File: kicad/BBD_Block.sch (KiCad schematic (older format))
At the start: 70 parts, among them U301 MN3102, U302 MN3102, U303 MN3205, U304 MN3205, U305 ADG619BRMZ, U306 MN3102, U307 MN3102, U308 MN3205, U309 MN3205, U310 ADG619BRMZ

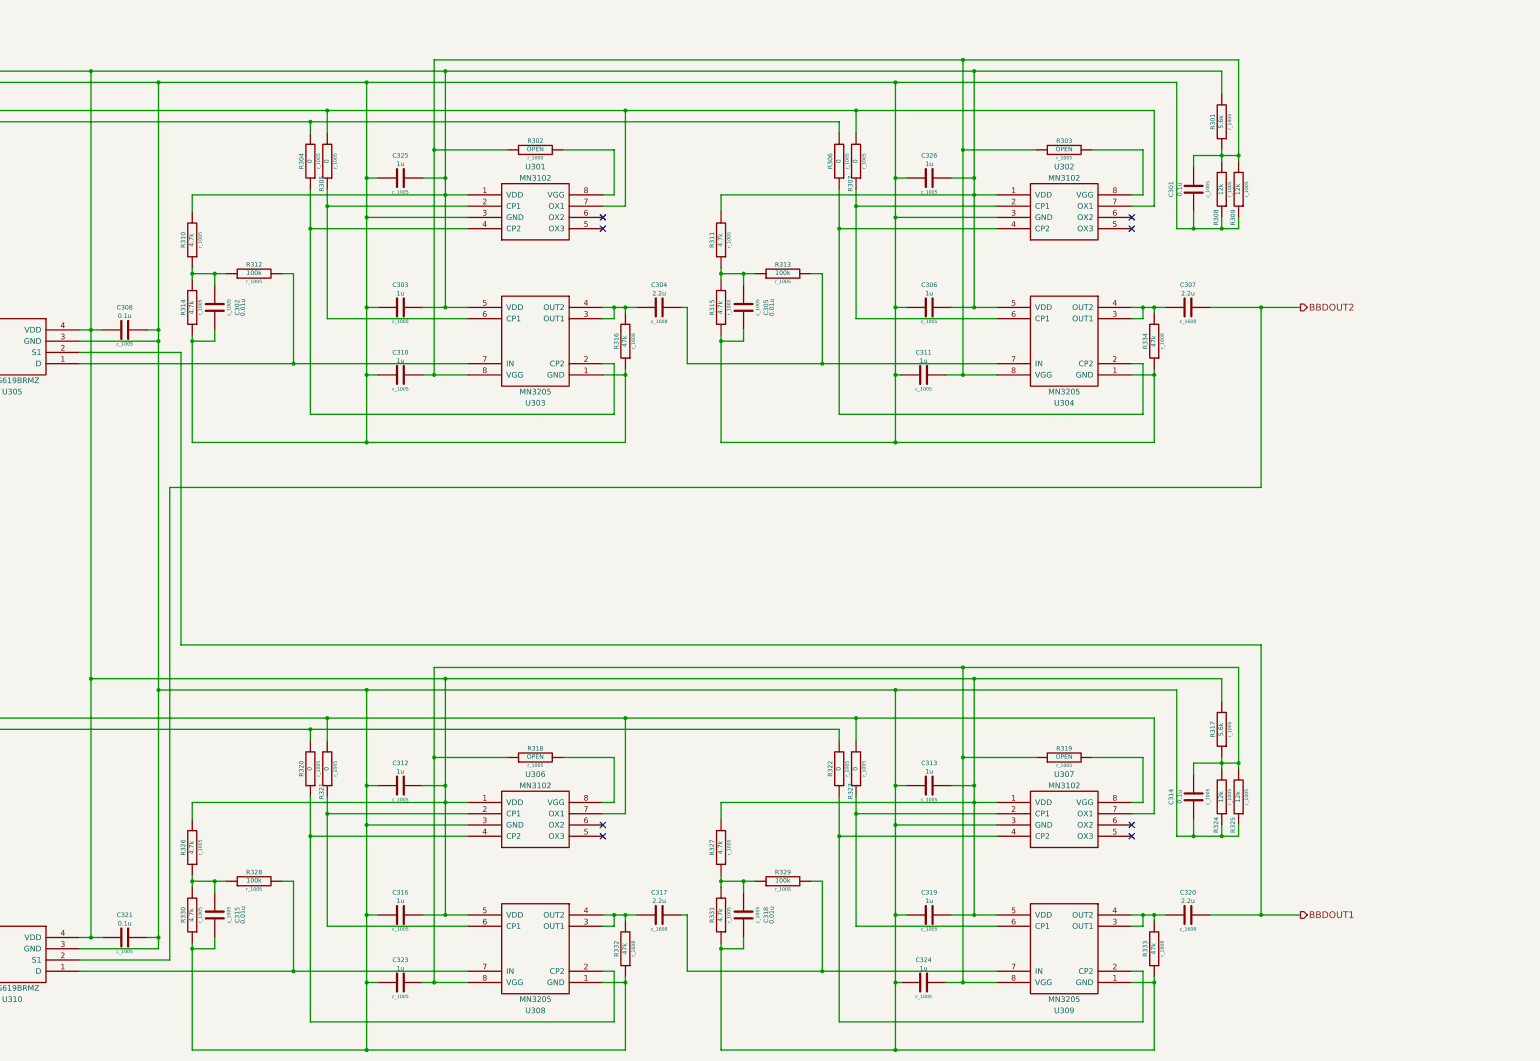
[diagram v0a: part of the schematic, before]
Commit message: Add: compander sch&pcb mod: constants
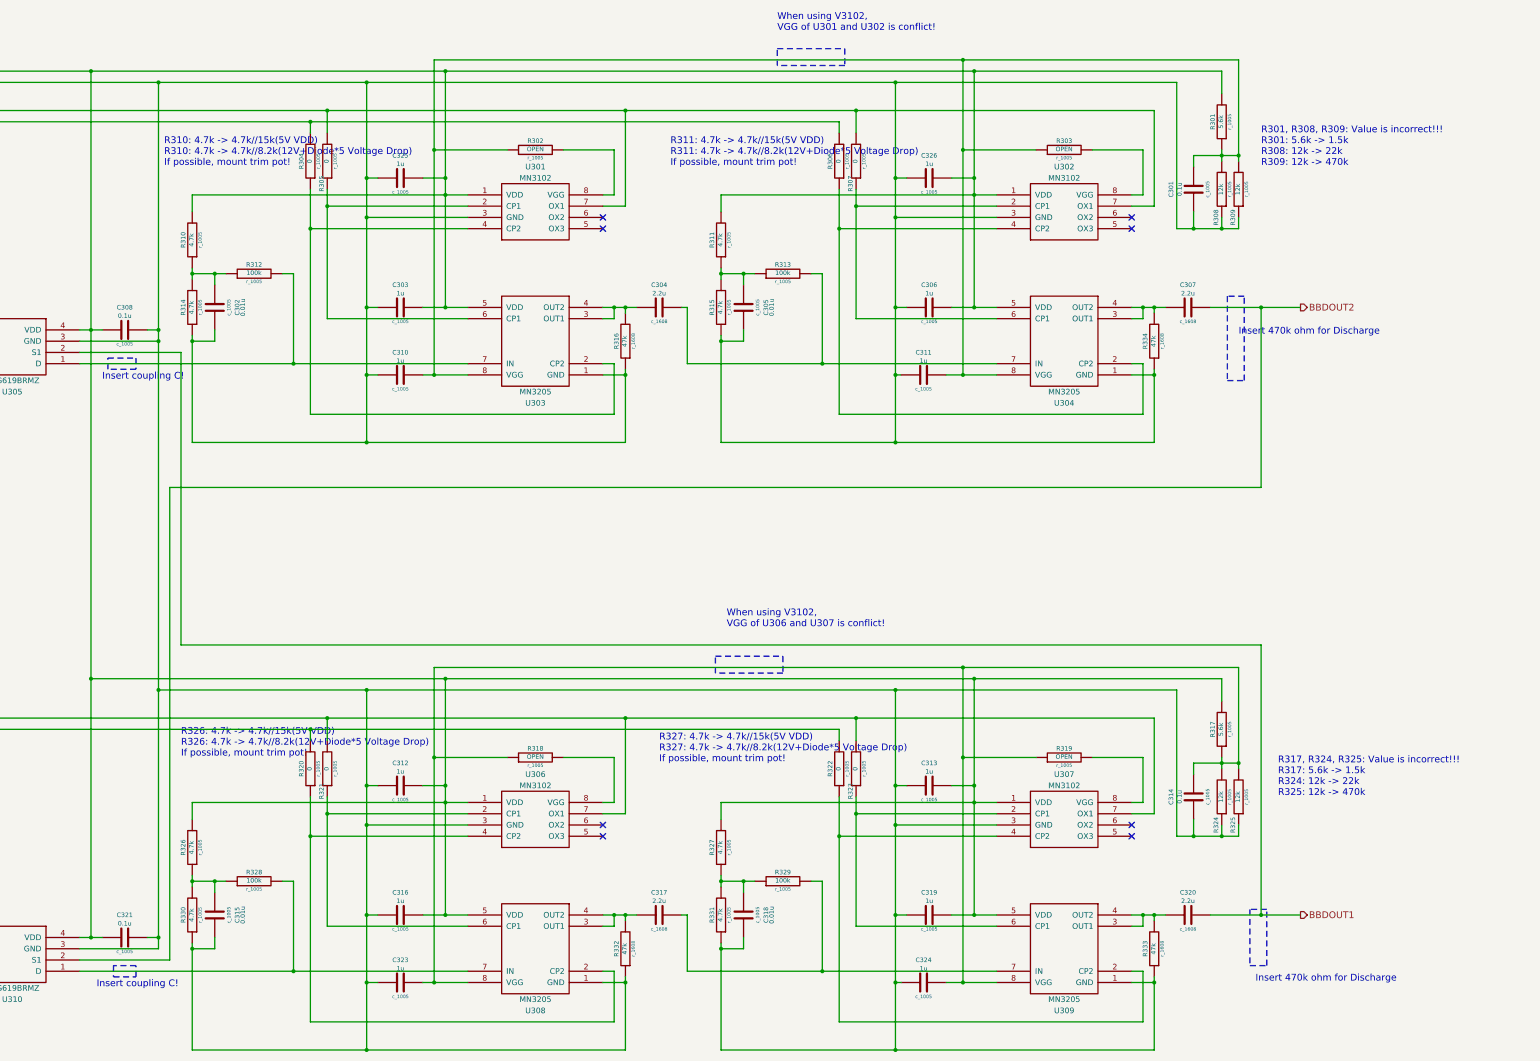
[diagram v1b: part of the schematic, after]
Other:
- note added: "Insert 470k ohm for Discharge"
- note added: "Insert coupling C!"
- note added: "R301, R308, R309: Value is incorrect!!!\nR301: 5.6k -> 1.5k\nR308: 12k -> 22k\nR309: 12k -> 470k"
- note added: "R310: 4.7k -> 4.7k//15k(5V VDD)\nR310: 4.7k -> 4.7k//8.2k(12V+Diode*5 Voltage Drop)\nIf possible, mount trim pot!\n"
- note added: "R311: 4.7k -> 4.7k//15k(5V VDD)\nR311: 4.7k -> 4.7k//8.2k(12V+Diode*5 Voltage Drop)\nIf possible, mount trim pot!\n"
- note added: "R317, R324, R325: Value is incorrect!!!\nR317: 5.6k -> 1.5k\nR324: 12k -> 22k\nR325: 12k -> 470k"
- note added: "R326: 4.7k -> 4.7k//15k(5V VDD)\nR326: 4.7k -> 4.7k//8.2k(12V+Diode*5 Voltage Drop)\nIf possible, mount trim pot!\n"
- note added: "R327: 4.7k -> 4.7k//15k(5V VDD)\nR327: 4.7k -> 4.7k//8.2k(12V+Diode*5 Voltage Drop)\nIf possible, mount trim pot!\n"
- note added: "When using V3102, \nVGG of U301 and U302 is conflict!"
- note added: "When using V3102, \nVGG of U306 and U307 is conflict!"
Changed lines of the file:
@@
 LIBS:jrc
 LIBS:rohm
+LIBS:temp
+LIBS:alps
+LIBS:on_semiconductor
 LIBS:AnalogDelay-cache
 EELAYER 27 0
@@
 Sheet 3 6
 Title ""
-Date "15 dec 2013"
+Date "30 apr 2014"
 Rev ""
 Comp ""
@@
 Connection ~ 4800 8950
 Wire Wire Line
-	4700 8950 4800 8950
+	4800 8950 4700 8950
 Connection ~ 4200 8950
 Connection ~ 2200 3750
@@
 	14000 7900 14000 8050
 Wire Wire Line
-	7550 2550 6650 2550
+	6650 2550 7550 2550
 Wire Wire Line
 	4100 3750 5000 3750
@@
 Connection ~ 4800 3650
 Wire Wire Line
-	4100 3650 4800 3650
+	4800 3650 4100 3650
 Connection ~ 4800 3550
 Wire Wire Line
@@
 	13850 6750 13850 8050
 Wire Wire Line
-	14250 7950 14250 8050
+	14250 8050 14250 7950
 Wire Wire Line
 	13850 8050 14400 8050
@@
 Connection ~ 6300 2450
 Wire Wire Line
-	6150 1800 6150 1700
+	6150 1700 6150 1800
 Wire Wire Line
 	1150 1700 10850 1700
 Wire Wire Line
-	6300 1800 6300 1600
+	6300 1600 6300 1800
 Wire Wire Line
 	1150 1600 13650 1600
@@
 	13850 1350 13850 2650
 Wire Wire Line
-	14250 2550 14250 2650
+	14250 2650 14250 2550
 Wire Wire Line
 	13850 2650 14400 2650
@@
 	1550 7100 10850 7100
 Wire Wire Line
-	11000 7200 11000 7000
+	11000 7000 11000 7200
 Wire Wire Line
 	1700 7000 13650 7000
@@
 Connection ~ 8950 1600
 Connection ~ 6150 1700
+Text Notes 14750 7700 0    60   ~ 0
+R317, R324, R325: Value is incorrect!!!\nR317: 5.6k -> 1.5k\nR324: 12k -> 22k\nR325: 12k -> 470k
+Text Notes 9350 2100 0    60   ~ 0
+R311: 4.7k -> 4.7k//15k(5V VDD)\nR311: 4.7k -> 4.7k//8.2k(12V+Diode*5 Voltage Drop)\nIf possible, mount trim pot!\n
+Wire Notes Line
+	10300 1050 10900 1050
+Wire Notes Line
+	10900 1050 10900 1200
+Wire Notes Line
+	10900 1200 10300 1200
+Wire Notes Line
+	10300 1200 10300 1050
+Text Notes 14600 2100 0    60   ~ 0
+R301, R308, R309: Value is incorrect!!!\nR301: 5.6k -> 1.5k\nR308: 12k -> 22k\nR309: 12k -> 470k
+Text Notes 10300 900  0    60   ~ 0
+When using V3102, \nVGG of U301 and U302 is conflict!
+Wire Notes Line
+	9750 6450 10350 6450
+Wire Notes Line
+	10350 6450 10350 6600
+Wire Notes Line
+	9750 6600 9750 6450
+Text Notes 9850 6200 0    60   ~ 0
+When using V3102, \nVGG of U306 and U307 is conflict!
+Wire Notes Line
+	10350 6600 9750 6600
+Wire Notes Line
+	4350 3800 4600 3800
+Wire Notes Line
+	4600 3800 4600 3900
+Wire Notes Line
+	4600 3900 4350 3900
+Wire Notes Line
+	4350 3900 4350 3800
+Text Notes 4300 4000 0    60   ~ 0
+Insert coupling C!
+Text Notes 9250 7400 0    60   ~ 0
+R327: 4.7k -> 4.7k//15k(5V VDD)\nR327: 4.7k -> 4.7k//8.2k(12V+Diode*5 Voltage Drop)\nIf possible, mount trim pot!\n
+Text Notes 5000 7350 0    60   ~ 0
+R326: 4.7k -> 4.7k//15k(5V VDD)\nR326: 4.7k -> 4.7k//8.2k(12V+Diode*5 Voltage Drop)\nIf possible, mount trim pot!\n
+Text Notes 4850 2100 0    60   ~ 0
+R310: 4.7k -> 4.7k//15k(5V VDD)\nR310: 4.7k -> 4.7k//8.2k(12V+Diode*5 Voltage Drop)\nIf possible, mount trim pot!\n
+Wire Notes Line
+	14500 8700 14500 9200
+Wire Notes Line
+	14500 9200 14650 9200
+Wire Notes Line
+	14650 9200 14650 8700
+Wire Notes Line
+	14650 8700 14500 8700
+Text Notes 14550 9350 0    60   ~ 0
+Insert 470k ohm for Discharge
+Text Notes 14400 3600 0    60   ~ 0
+Insert 470k ohm for Discharge
+Wire Notes Line
+	14300 3250 14300 4000
+Wire Notes Line
+	14300 4000 14450 4000
+Wire Notes Line
+	14450 4000 14450 3250
+Wire Notes Line
+	14450 3250 14300 3250
+Text Notes 4250 9400 0    60   ~ 0
+Insert coupling C!
+Wire Notes Line
+	4400 9200 4400 9300
+Wire Notes Line
+	4400 9300 4600 9300
+Wire Notes Line
+	4600 9300 4600 9200
+Wire Notes Line
+	4600 9200 4400 9200
 $EndSCHEMATC

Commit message: mod: Schematics
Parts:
- removed R301, R317: 5.6k, r_1005, symbol R_1005
- removed R302, R303, R318, R319: OPEN, r_1005, symbol R_1005
- removed R304, R305, R306, R307, R320, R321, R322, R323: 0, r_1005, symbol R_1005
- removed R308, R309, R324, R325: 12k, r_1005, symbol R_1005
- added C? (x2): 2.2u, c_1608, symbol C_1608
- added C? (x2): 0.1u, c_1005, symbol C_1005
- added R? (x2): 470k, r_1608, symbol R_1608
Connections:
- net AGND: now also C?.1, C?.1, R?.1, R?.1
- net BBDOUT1: now also R?.2
- net BBDOUT2: now also R?.2
- net at C314.2, C324.2, U309.8 (VGG): now also U307.8 (VGG); no longer C323.2, U308.8 (VGG)
- net at R328.2, U308.7 (IN): now also C?.2; no longer U310.1 (D)
- net at R312.2, U303.7 (IN): now also C?.2; no longer U305.1 (D)
- net at C301.2, C311.2, U304.8 (VGG): now also U302.8 (VGG); no longer C310.2, U303.8 (VGG)
- net at U306.8 (VGG): now also C323.2, U308.8 (VGG), C?.2
- net at U301.8 (VGG): now also C310.2, U303.8 (VGG), C?.2
- new net: C?.1, U310.1 (D)
- new net: C?.1, U305.1 (D)
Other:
- note added: "BBD output gain attenuate\n"
- note added: "If possible, mount trim pot!\n"
- note removed: "Insert 470k ohm for Discharge"
- note removed: "Insert coupling C!"
- note removed: "R301, R308, R309: Value is incorrect!!!\nR301: 5.6k -> 1.5k\nR308: 12k -> 22k\nR309: 12k -> 470k"
- note removed: "R317, R324, R325: Value is incorrect!!!\nR317: 5.6k -> 1.5k\nR324: 12k -> 22k\nR325: 12k -> 470k"
- note removed: "When using V3102, \nVGG of U301 and U302 is conflict!"
- note removed: "When using V3102, \nVGG of U306 and U307 is conflict!"
- moved on the sheet: C301, C302, C303, C308, C309, C310, C312, C314, C315, C316, C321, C322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
